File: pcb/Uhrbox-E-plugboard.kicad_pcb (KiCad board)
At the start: 2 copper layers, 172 x 65 mm, 21 parts, among them J1 Conn_01x20_Female, J10 Conn_01x01_MountingPin, J11 Conn_01x01_MountingPin, J13 Conn_01x01_MountingPin, J14 Conn_01x01_MountingPin, J15 Conn_01x01_MountingPin, J16 Conn_01x01_MountingPin, J17 Conn_01x01_MountingPin, J18 Conn_01x01_MountingPin, J19 Conn_01x01_MountingPin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

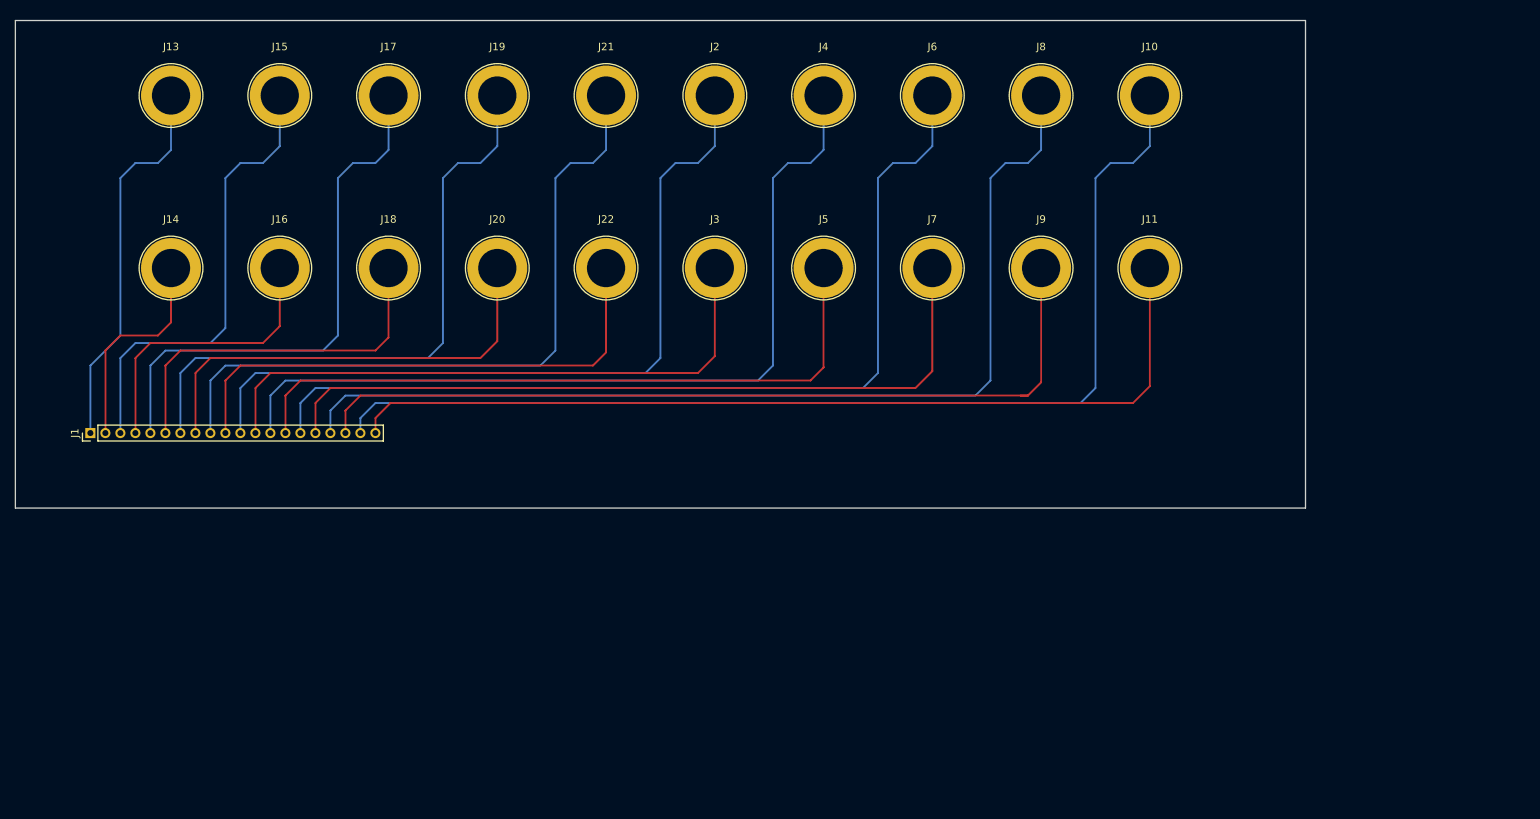
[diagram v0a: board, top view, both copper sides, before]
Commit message: Uhrbord-E plugboard PCB sent to manufacturing
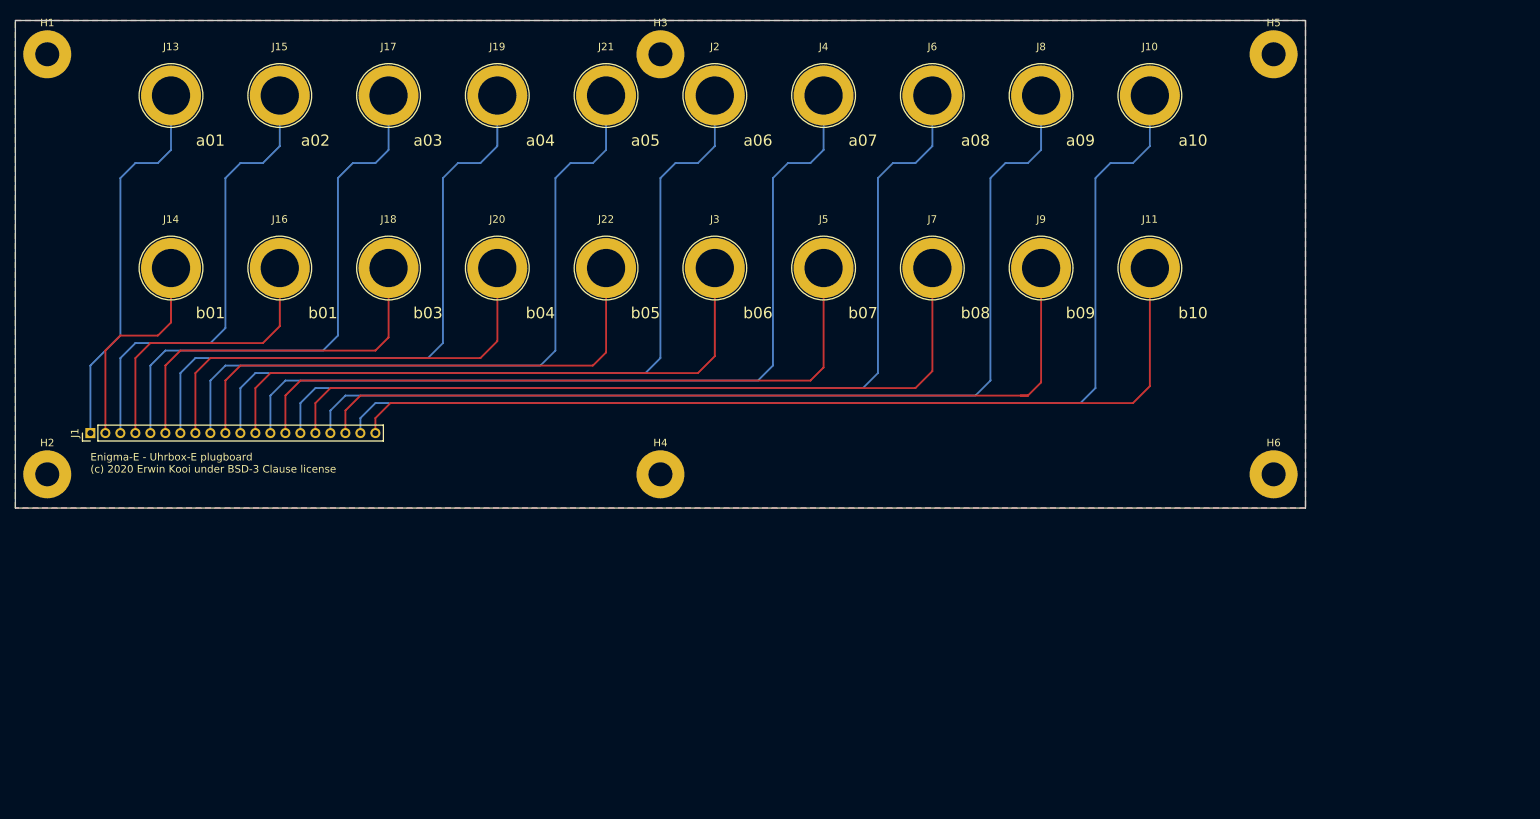
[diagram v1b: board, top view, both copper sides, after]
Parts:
- added H1: MountingHole_Pad, MountingHole:MountingHole_3.2mm_M3_Pad, F.Cu at (4.25, 4.50)
- added H2: MountingHole_Pad, MountingHole:MountingHole_3.2mm_M3_Pad, F.Cu at (4.25, 60.5)
- added H3: MountingHole_Pad, MountingHole:MountingHole_3.2mm_M3_Pad, F.Cu at (86.0, 4.50)
- added H4: MountingHole_Pad, MountingHole:MountingHole_3.2mm_M3_Pad, F.Cu at (86.0, 60.5)
- added H5: MountingHole_Pad, MountingHole:MountingHole_3.2mm_M3_Pad, F.Cu at (167.8, 4.50)
- added H6: MountingHole_Pad, MountingHole:MountingHole_3.2mm_M3_Pad, F.Cu at (167.8, 60.5)
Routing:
- added copper zone on B.Cu, net GND
- added copper zone on F.Cu, net GND
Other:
- board text added: "Enigma-E - Uhrbox-E plugboard (c) 2020 Erwin Kooi under BSD-3 Clause license"
- board text added: "a01"
- board text added: "a02"
- board text added: "a03"
- board text added: "a04"
- board text added: "a05"
- board text added: "a06"
- board text added: "a07"
- board text added: "a08"
- board text added: "a09"
- board text added: "a10"
- board text added: "b01"
- board text added: "b03"
- board text added: "b04"
- board text added: "b05"
- board text added: "b06"
- board text added: "b07"
- board text added: "b08"
- board text added: "b09"
- board text added: "b10"
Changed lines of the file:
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@@
   (general
     (thickness 1.6)
-    (drawings 4)
+    (drawings 25)
     (tracks 140)
     (zones 0)
-    (modules 21)
-    (nets 21)
+    (modules 27)
+    (nets 22)
   )
   (page A4)
@@
     (mod_text_size 1 1)
     (mod_text_width 0.15)
-    (pad_size 8 8)
-    (pad_drill 5.1)
+    (pad_size 3.2 3.2)
+    (pad_drill 3.2)
     (pad_to_mask_clearance 0)
     (aux_axis_origin 0 0)
     (visible_elements FFFFFF7F)
     (pcbplotparams
-      (layerselection 0x010fc_ffffffff)
+      (layerselection 0x010f0_ffffffff)
       (usegerberextensions false)
       (usegerberattributes true)
@@
       (psa4output false)
       (plotreference true)
-      (plotvalue true)
+      (plotvalue false)
       (plotinvisibletext false)
       (padsonsilk false)
@@
       (outputformat 1)
       (mirror false)
-      (drillshape 1)
+      (drillshape 0)
       (scaleselection 1)
-      (outputdirectory ""))
+      (outputdirectory "gerber/"))
   )
   (net 0 "")
@@
   (net 19 "Net-(J1-Pad2)")
   (net 20 "Net-(J1-Pad1)")
+  (net 21 GND)
   (net_class Default "This is the default net class."
     (clearance 0.2)
@@
     (uvia_dia 0.3)
     (uvia_drill 0.1)
+    (add_net GND)
     (add_net "Net-(J1-Pad1)")
     (add_net "Net-(J1-Pad10)")
@@
     (add_net "Net-(J1-Pad9)")
   )
+  (module MountingHole:MountingHole_3.2mm_M3_Pad (layer F.Cu)
+    (at 167.75 60.5)
+    (descr "Mounting Hole 3.2mm, M3")
+    (tags "mounting hole 3.2mm m3")
+    (attr virtual)
+    (fp_text reference H6 (at 0 -4.2) (layer F.SilkS)
+      (effects (font (size 1 1) (thickness 0.15)))
+    )
+    (fp_text value MountingHole_Pad (at 0 4.2) (layer F.Fab)
+      (effects (font (size 1 1) (thickness 0.15)))
+    )
+    (fp_circle (center 0 0) (end 3.2 0) (layer Cmts.User) (width 0.15))
+    (fp_circle (center 0 0) (end 3.45 0) (layer F.CrtYd) (width 0.05))
+    (fp_text user %R (at 0.3 0) (layer F.Fab)
+      (effects (font (size 1 1) (thickness 0.15)))
+    )
+    (pad 1 thru_hole circle (at 0 0) (size 6.4 6.4) (drill 3.2) (layers *.Cu *.Mask)
+      (net 21 GND))
+  )
+  (module MountingHole:MountingHole_3.2mm_M3_Pad (layer F.Cu)
+    (at 167.75 4.5)
+    (descr "Mounting Hole 3.2mm, M3")
+    (tags "mounting hole 3.2mm m3")
+    (attr virtual)
+    (fp_text reference H5 (at 0 -4.2) (layer F.SilkS)
+      (effects (font (size 1 1) (thickness 0.15)))
+    )
+    (fp_text value MountingHole_Pad (at 0 4.2) (layer F.Fab)
+      (effects (font (size 1 1) (thickness 0.15)))
+    )
+    (fp_circle (center 0 0) (end 3.2 0) (layer Cmts.User) (width 0.15))
+    (fp_circle (center 0 0) (end 3.45 0) (layer F.CrtYd) (width 0.05))
+    (fp_text user %R (at 0.3 0) (layer F.Fab)
+      (effects (font (size 1 1) (thickness 0.15)))
+    )
+    (pad 1 thru_hole circle (at 0 0) (size 6.4 6.4) (drill 3.2) (layers *.Cu *.Mask)
+      (net 21 GND))
+  )
+  (module MountingHole:MountingHole_3.2mm_M3_Pad (layer F.Cu)
+    (at 86 60.5)
+    (descr "Mounting Hole 3.2mm, M3")
+    (tags "mounting hole 3.2mm m3")
+    (attr virtual)
+    (fp_text reference H4 (at 0 -4.2) (layer F.SilkS)
+      (effects (font (size 1 1) (thickness 0.15)))
+    )
+    (fp_text value MountingHole_Pad (at 0 4.2) (layer F.Fab)
+      (effects (font (size 1 1) (thickness 0.15)))
+    )
+    (fp_circle (center 0 0) (end 3.2 0) (layer Cmts.User) (width 0.15))
+    (fp_circle (center 0 0) (end 3.45 0) (layer F.CrtYd) (width 0.05))
+    (fp_text user %R (at 0.3 0) (layer F.Fab)
+      (effects (font (size 1 1) (thickness 0.15)))
+    )
+    (pad 1 thru_hole circle (at 0 0) (size 6.4 6.4) (drill 3.2) (layers *.Cu *.Mask)
+      (net 21 GND))
+  )
+  (module MountingHole:MountingHole_3.2mm_M3_Pad (layer F.Cu)
+    (at 86 4.5)
+    (descr "Mounting Hole 3.2mm, M3")
+    (tags "mounting hole 3.2mm m3")
+    (attr virtual)
+    (fp_text reference H3 (at 0 -4.2) (layer F.SilkS)
+      (effects (font (size 1 1) (thickness 0.15)))
+    )
+    (fp_text value MountingHole_Pad (at 0 4.2) (layer F.Fab)
+      (effects (font (size 1 1) (thickness 0.15)))
+    )
+    (fp_circle (center 0 0) (end 3.2 0) (layer Cmts.User) (width 0.15))
+    (fp_circle (center 0 0) (end 3.45 0) (layer F.CrtYd) (width 0.05))
+    (fp_text user %R (at 0.3 0) (layer F.Fab)
+      (effects (font (size 1 1) (thickness 0.15)))
+    )
+    (pad 1 thru_hole circle (at 0 0) (size 6.4 6.4) (drill 3.2) (layers *.Cu *.Mask)
+      (net 21 GND))
+  )
+  (module MountingHole:MountingHole_3.2mm_M3_Pad (layer F.Cu)
+    (at 4.25 60.5)
+    (descr "Mounting Hole 3.2mm, M3")
+    (tags "mounting hole 3.2mm m3")
+    (attr virtual)
+    (fp_text reference H2 (at 0 -4.2) (layer F.SilkS)
+      (effects (font (size 1 1) (thickness 0.15)))
+    )
+    (fp_text value MountingHole_Pad (at 0 4.2) (layer F.Fab)
+      (effects (font (size 1 1) (thickness 0.15)))
+    )
+    (fp_circle (center 0 0) (end 3.2 0) (layer Cmts.User) (width 0.15))
+    (fp_circle (center 0 0) (end 3.45 0) (layer F.CrtYd) (width 0.05))
+    (fp_text user %R (at 0.3 0) (layer F.Fab)
+      (effects (font (size 1 1) (thickness 0.15)))
+    )
+    (pad 1 thru_hole circle (at 0 0) (size 6.4 6.4) (drill 3.2) (layers *.Cu *.Mask)
+      (net 21 GND))
+  )
+  (module MountingHole:MountingHole_3.2mm_M3_Pad (layer F.Cu)
+    (at 4.25 4.5)
+    (descr "Mounting Hole 3.2mm, M3")
+    (tags "mounting hole 3.2mm m3")
+    (attr virtual)
+    (fp_text reference H1 (at 0 -4.2) (layer F.SilkS)
+      (effects (font (size 1 1) (thickness 0.15)))
+    )
+    (fp_text value MountingHole_Pad (at 0 4.2) (layer F.Fab)
+      (effects (font (size 1 1) (thickness 0.15)))
+    )
+    (fp_circle (center 0 0) (end 3.2 0) (layer Cmts.User) (width 0.15))
+    (fp_circle (center 0 0) (end 3.45 0) (layer F.CrtYd) (width 0.05))
+    (fp_text user %R (at 0.3 0) (layer F.Fab)
+      (effects (font (size 1 1) (thickness 0.15)))
+    )
+    (pad 1 thru_hole circle (at 0 0) (size 6.4 6.4) (drill 3.2) (layers *.Cu *.Mask)
+      (net 21 GND))
+  )
   (module Uhrbox-E-plugboard:Banana_Jack_1Pin_26mm (layer F.Cu)
     (at 35.25 10)
@@
       (effects (font (size 1 1) (thickness 0.15)))
     )
-    (fp_text value Conn_01x20_Female (at 0 40.06 90) (layer F.Fab)
+    (fp_text value Conn_01x20_Female (at -3 19 180) (layer F.Fab)
       (effects (font (size 1 1) (thickness 0.15)))
     )
@@
       (rotate (xyz 0 0 0))
     )
+  )
+  (gr_text "Enigma-E - Uhrbox-E plugboard\n(c) 2020 Erwin Kooi under BSD-3 Clause license" (at 10 59) (layer F.SilkS)
+    (effects (font (size 1 1) (thickness 0.15)) (justify left))
+  )
+  (gr_text b01 (at 26 39) (layer F.SilkS)
+    (effects (font (size 1.5 1.5) (thickness 0.3)))
+  )
+  (gr_text b01 (at 41 39) (layer F.SilkS)
+    (effects (font (size 1.5 1.5) (thickness 0.3)))
+  )
+  (gr_text b03 (at 55 39) (layer F.SilkS)
+    (effects (font (size 1.5 1.5) (thickness 0.3)))
+  )
+  (gr_text b04 (at 70 39) (layer F.SilkS)
+    (effects (font (size 1.5 1.5) (thickness 0.3)))
+  )
+  (gr_text b05 (at 84 39) (layer F.SilkS)
+    (effects (font (size 1.5 1.5) (thickness 0.3)))
+  )
+  (gr_text b06 (at 99 39) (layer F.SilkS)
+    (effects (font (size 1.5 1.5) (thickness 0.3)))
+  )
+  (gr_text b07 (at 113 39) (layer F.SilkS)
+    (effects (font (size 1.5 1.5) (thickness 0.3)))
+  )
+  (gr_text b08 (at 128 39) (layer F.SilkS)
+    (effects (font (size 1.5 1.5) (thickness 0.3)))
+  )
+  (gr_text b09 (at 142 39) (layer F.SilkS)
+    (effects (font (size 1.5 1.5) (thickness 0.3)))
+  )
+  (gr_text b10 (at 157 39) (layer F.SilkS)
+    (effects (font (size 1.5 1.5) (thickness 0.3)))
+  )
+  (gr_text a10 (at 157 16) (layer F.SilkS)
+    (effects (font (size 1.5 1.5) (thickness 0.3)))
+  )
+  (gr_text a09 (at 142 16) (layer F.SilkS)
+    (effects (font (size 1.5 1.5) (thickness 0.3)))
+  )
+  (gr_text a08 (at 128 16) (layer F.SilkS)
+    (effects (font (size 1.5 1.5) (thickness 0.3)))
+  )
+  (gr_text a07 (at 113 16) (layer F.SilkS)
+    (effects (font (size 1.5 1.5) (thickness 0.3)))
+  )
+  (gr_text a06 (at 99 16) (layer F.SilkS)
+    (effects (font (size 1.5 1.5) (thickness 0.3)))
+  )
+  (gr_text a05 (at 84 16) (layer F.SilkS)
+    (effects (font (size 1.5 1.5) (thickness 0.3)))
+  )
+  (gr_text a04 (at 70 16) (layer F.SilkS)
+    (effects (font (size 1.5 1.5) (thickness 0.3)))
+  )
+  (gr_text a03 (at 55 16) (layer F.SilkS)
+    (effects (font (size 1.5 1.5) (thickness 0.3)))
+  )
+  (gr_text a02 (at 40 16) (layer F.SilkS)
+    (effects (font (size 1.5 1.5) (thickness 0.3)))
+  )
+  (gr_text a01 (at 26 16) (layer F.SilkS)
+    (effects (font (size 1.5 1.5) (thickness 0.3)))
   )
   (gr_line (start 0 0) (end 0 65) (layer Edge.Cuts) (width 0.1))
@@
   (segment (start 19 19) (end 20.75 17.25) (width 0.25) (layer B.Cu) (net 20))
   (segment (start 10 55) (end 10 46) (width 0.25) (layer B.Cu) (net 20))
+  (zone (net 21) (net_name GND) (layer F.Cu) (hatch edge 0.508)
+    (connect_pads (clearance 0.508))
+    (min_thickness 0.254)
+    (fill yes (arc_segments 32) (thermal_gap 0.508) (thermal_bridge_width 0.508))
+    (polygon
+      (pts
+        (xy 172 65) (xy 0 65) (xy 0 0) (xy 172 0)
+      )
+    )
+  )
+  (zone (net 21) (net_name GND) (layer B.Cu) (hatch edge 0.508)
+    (connect_pads (clearance 0.508))
+    (min_thickness 0.254)
+    (fill yes (arc_segments 32) (thermal_gap 0.508) (thermal_bridge_width 0.508))
+    (polygon
+      (pts
+        (xy 172 65) (xy 0 65) (xy 0 0) (xy 172 0)
+      )
+    )
+  )
 )

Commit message: Changed header to 2.54mm and sent to manufacturing
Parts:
- J1: footprint Connector_PinHeader_2.00mm:PinHeader_1x20_P2.00mm_Vertical -> Connector_PinHeader_2.54mm:PinHeader_1x20_P2.54mm_Vertical
- moved J1 55.2 mm to (43.2, 99.1)
- moved H5 49.0 mm to (197.0, 43.9)
- moved J10 49.0 mm to (180.5, 49.4)
- moved J4 49.0 mm to (137.0, 49.4)
- moved J6 49.0 mm to (151.5, 49.4)
- moved J8 49.0 mm to (166.0, 49.4)
- moved H1 49.0 mm to (33.5, 43.9)
- moved H2 49.0 mm to (33.5, 99.9)
- moved H3 49.0 mm to (115.2, 43.9)
- moved H6 49.0 mm to (197.0, 99.9)
- moved J11 49.0 mm to (180.5, 72.4)
- moved J13 49.0 mm to (50.0, 49.4)
- moved J14 49.0 mm to (50.0, 72.4)
- moved J15 49.0 mm to (64.5, 49.4)
- moved J17 49.0 mm to (79.0, 49.4)
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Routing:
- net Net-(J1-Pad20): track 122.8 -> 114.2 mm
- net Net-(J1-Pad18): track 113.6 -> 105.0 mm
- net Net-(J1-Pad16): track 101.8 -> 95.2 mm
- net Net-(J1-Pad19): track 145.4 -> 138.9 mm
- net Net-(J1-Pad17): track 135.2 -> 129.5 mm
- net Net-(J1-Pad14): track 91.6 -> 86.1 mm
- net Net-(J1-Pad1): track 51.2 -> 55.6 mm
- net Net-(J1-Pad15): track 124.4 -> 120.1 mm
- net Net-(J1-Pad12): track 80.8 -> 77.0 mm
- net Net-(J1-Pad13): track 114.2 -> 110.7 mm
- net Net-(J1-Pad10): track 70.6 -> 67.1 mm
- net Net-(J1-Pad11): track 103.4 -> 101.2 mm
- net Net-(J1-Pad3): track 61.4 -> 63.6 mm
- net Net-(J1-Pad8): track 59.8 -> 58.0 mm
- net Net-(J1-Pad6): track 49.6 -> 48.2 mm
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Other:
- board text added: "b02"
